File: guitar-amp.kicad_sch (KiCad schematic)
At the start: 62 parts, among them J1 Speaker Output, J2 Input, J3 AC Mains, J4 Screw_Terminal_01x02, J5 Screw_Terminal_01x02, J6 Screw_Terminal_01x02, SW1 SW_SPST, T1 Transformer_1P_1S, T2 Transformer_1P_2S

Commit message: Add lamp and test points
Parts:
- added J7: Lamp, TerminalBlock_RND:TerminalBlock_RND_205-00001_1x02_P5.00mm_Horizontal, symbol Connector:Screw_Terminal_01x02
- added TP1, TP10, TP2, TP3, TP4, TP5, TP6, TP7, TP8, TP9: TestPoint_Probe, TestPoint:TestPoint_Pad_D2.5mm, symbol Connector:TestPoint_Probe
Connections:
- net AC_L: now also J7.1 (Pin_1)
- net AC_N: now also J7.2 (Pin_2)
- net HighDC_227VDC: now also TP6.1
- net HighDC_241VDC: now also TP9.1
- net HighDC_OT: now also TP10.1
- net at C7.2, R11.2, R15.1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: now also TP2.1
- net at J2.T, R10.1, R13.1: now also TP1.1
- net at R12.2, R17.1, V2.7 (G): now also TP3.1
- net HighCurrentTrace1: now reaches J5.2 (Pin_2), R24.1, SW1.1 (A)
- net HighCurrentTrace2: now reaches R22.2, R24.2, SW1.2 (B), V1.4 (F1), V1.5 (F1), V2.4 (F1), V2.5 (F1), V3.4 (F1)
- net HighCurrentTrace2: now also TP7.1
- net at R9.1, V3.2 (G1): now also TP4.1
- net HighCurrentTrace3: now reaches J5.1 (Pin_1), R23.2, V1.9 (F2), V2.9 (F2), V3.5 (F2)
- net HighCurrentTrace3: now also TP8.1
- net at J1.1 (Pin_1), T1.4 (SB): now also TP5.1
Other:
- moved on the sheet: D1, J3, J4, J5, J6, T2

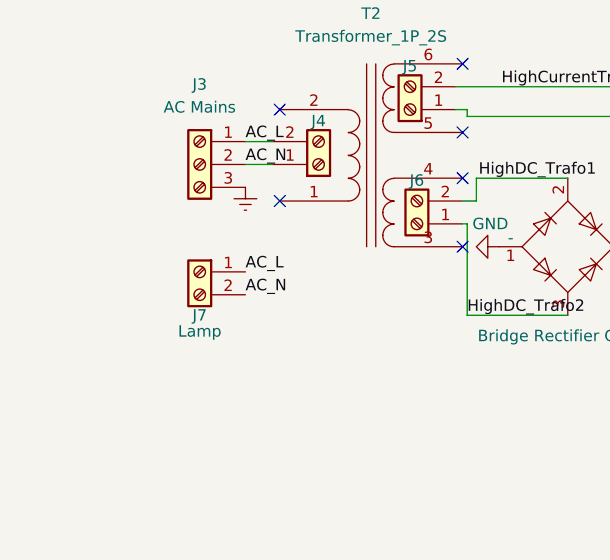
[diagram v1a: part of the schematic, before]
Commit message: Make the filament traces bigger
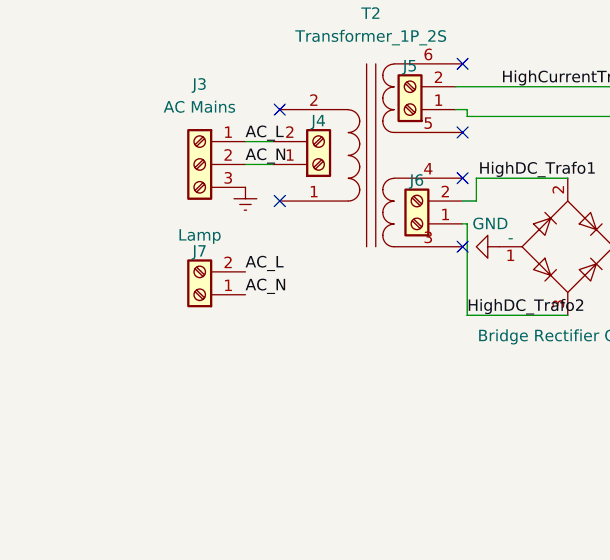
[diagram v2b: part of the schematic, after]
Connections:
- net AC_L: now also J7.2 (Pin_2); no longer J7.1 (Pin_1)
- net AC_N: now also J7.1 (Pin_1); no longer J7.2 (Pin_2)
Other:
- moved on the sheet: J7
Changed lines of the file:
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@@
     (pin "2")
   )
-  (symbol (lib_id "Connector:Screw_Terminal_01x02") (at 37.846 160.02 0) (mirror y) (unit 1)
+  (symbol (lib_id "Connector:Screw_Terminal_01x02") (at 37.846 162.56 180) (unit 1)
     (in_bom yes) (on_board yes)
-    (property "Reference" "J7" (id 0) (at 37.846 164.846 0))
-    (property "Value" "Lamp" (id 1) (at 37.846 166.624 0))
-    (property "Footprint" "TerminalBlock_RND:TerminalBlock_RND_205-00001_1x02_P5.00mm_Horizontal" (id 2) (at 37.846 160.02 0)
+    (property "Reference" "J7" (id 0) (at 37.846 157.734 0))
+    (property "Value" "Lamp" (id 1) (at 37.846 155.956 0))
+    (property "Footprint" "TerminalBlock_RND:TerminalBlock_RND_205-00001_1x02_P5.00mm_Horizontal" (id 2) (at 37.846 162.56 0)
       (effects (font (size 1.27 1.27)) hide)
     )
-    (property "Datasheet" "~" (id 3) (at 37.846 160.02 0)
+    (property "Datasheet" "~" (id 3) (at 37.846 162.56 0)
       (effects (font (size 1.27 1.27)) hide)
     )

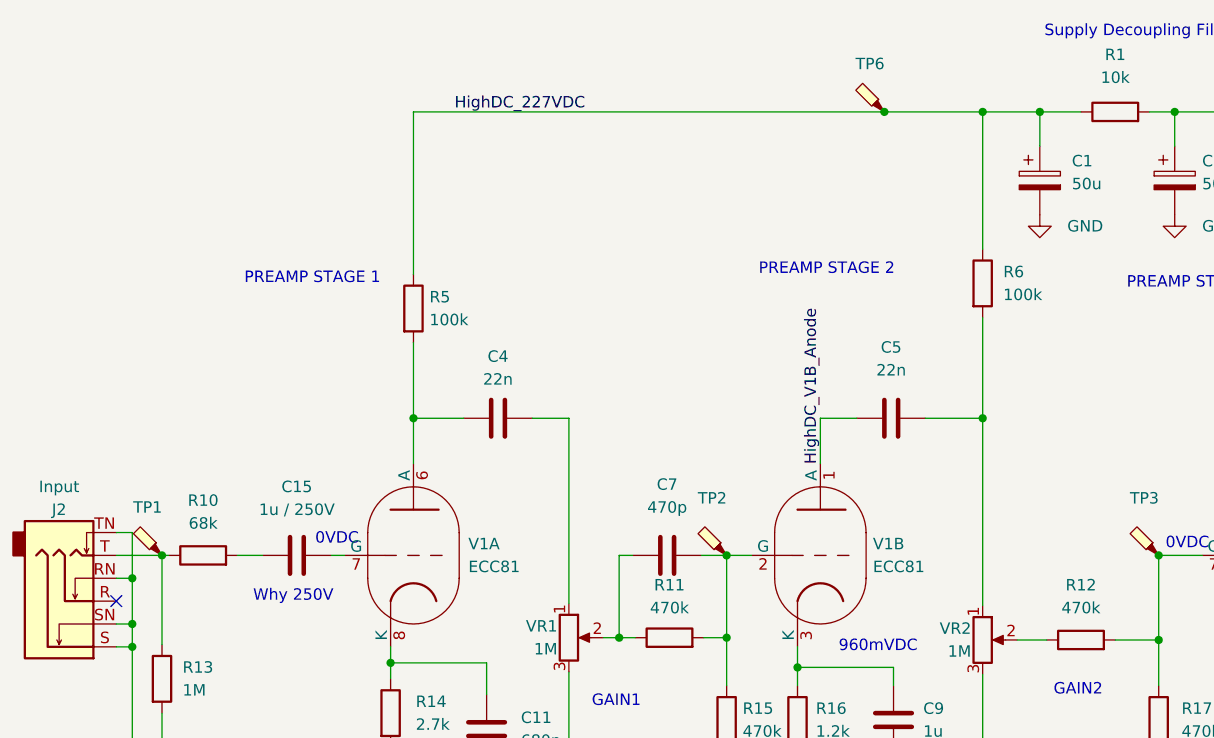
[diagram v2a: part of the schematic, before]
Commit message: Fix R6 and Remove C15
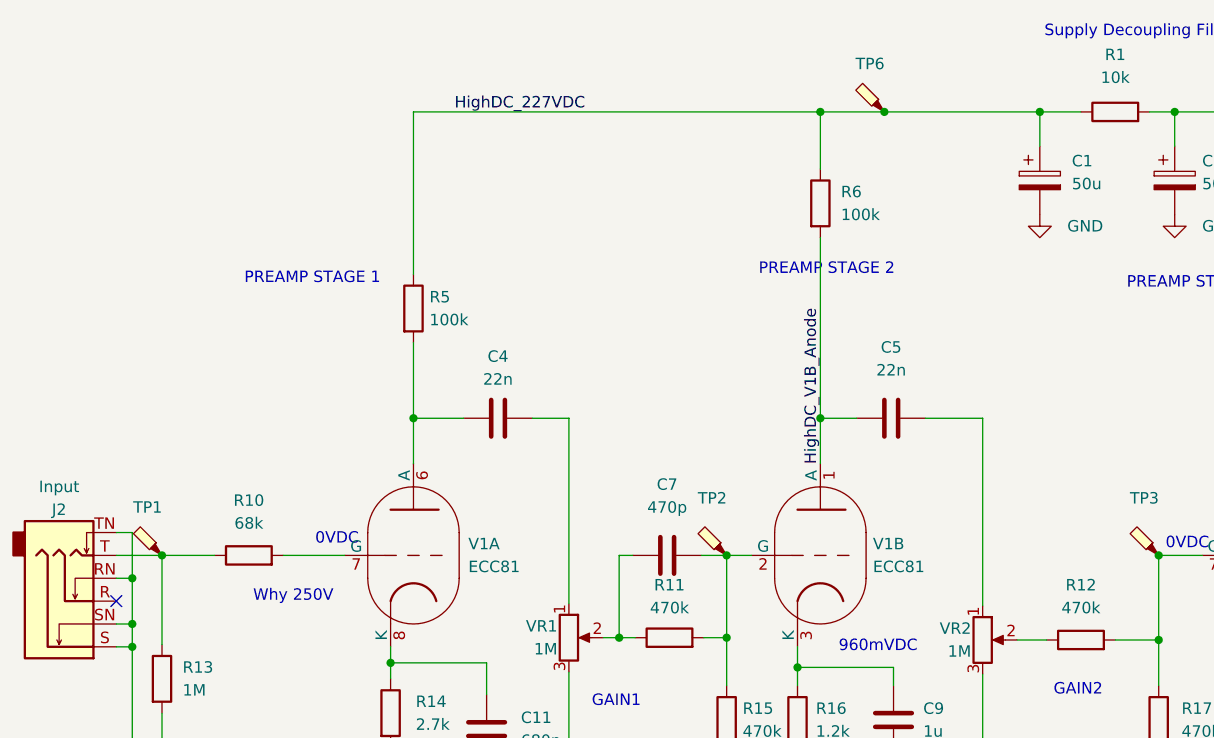
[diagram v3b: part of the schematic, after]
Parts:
- removed C15: 1u / 250V, Capacitor_THT:C_Rect_L27.0mm_W9.0mm_P23.00mm, symbol Device:C
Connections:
- net HighDC_V1B_Anode: now also R6.2
- net at R10.2: now also V1.7 (G)
- net at C5.2, VR2.1: no longer R6.2
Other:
- moved on the sheet: R10, R6
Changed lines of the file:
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@@
   (junction (at 125.476 110.49) (diameter 0) (color 0 0 0 0)
   )
-  (junction (at 125.476 68.58) (diameter 0) (color 0 0 0 0)
-  )
   (junction (at 188.976 139.446) (diameter 0) (color 0 0 0 0)
   )
@@
   (junction (at 146.812 34.544) (diameter 0) (color 0 0 0 0)
   )
-  (junction (at 125.476 34.544) (diameter 0) (color 0 0 0 0)
-  )
   (junction (at 235.458 83.82) (diameter 0) (color 0 0 0 0)
   )
@@
   (junction (at 104.902 96.266) (diameter 0) (color 0 0 0 0)
   )
+  (junction (at 107.442 34.544) (diameter 0) (color 0 0 0 0)
+  )
   (junction (at 34.29 110.49) (diameter 0) (color 0 0 0 0)
   )
@@
   )
   (junction (at 85.09 92.964) (diameter 0) (color 0 0 0 0)
+  )
+  (junction (at 107.442 68.58) (diameter 0) (color 0 0 0 0)
   )
   (junction (at 175.514 60.198) (diameter 0) (color 0 0 0 0)
@@
     (stroke (width 0) (type default) (color 0 0 0 0))
   )
-  (wire (pts (xy 53.086 83.82) (xy 54.61 83.82))
+  (wire (pts (xy 47.752 83.82) (xy 54.61 83.82))
     (stroke (width 0) (type default) (color 0 0 0 0))
   )
@@
     (stroke (width 0) (type default) (color 0 0 0 0))
   )
-  (wire (pts (xy 42.672 83.82) (xy 45.466 83.82))
-    (stroke (width 0) (type default) (color 0 0 0 0))
-  )
   (wire (pts (xy 115.824 155.448) (xy 121.666 155.448))
     (stroke (width 0) (type default) (color 0 0 0 0))
@@
     (stroke (width 0) (type default) (color 0 0 0 0))
   )
-  (wire (pts (xy 62.23 34.544) (xy 114.554 34.544))
+  (wire (pts (xy 62.23 34.544) (xy 107.442 34.544))
     (stroke (width 0) (type default) (color 0 0 0 0))
   )
@@
     (stroke (width 0) (type default) (color 0 0 0 0))
   )
-  (wire (pts (xy 114.554 34.544) (xy 125.476 34.544))
+  (wire (pts (xy 114.554 34.544) (xy 131.826 34.544))
     (stroke (width 0) (type default) (color 0 0 0 0))
   )
@@
     (stroke (width 0) (type default) (color 0 0 0 0))
   )
+  (wire (pts (xy 107.442 40.894) (xy 107.442 34.544))
+    (stroke (width 0) (type default) (color 0 0 0 0))
+  )
   (wire (pts (xy 67.056 154.686) (xy 67.564 154.686))
     (stroke (width 0) (type default) (color 0 0 0 0))
@@
     (stroke (width 0) (type default) (color 0 0 0 0))
   )
-  (wire (pts (xy 34.29 83.82) (xy 35.052 83.82))
+  (wire (pts (xy 34.29 83.82) (xy 40.132 83.82))
     (stroke (width 0) (type default) (color 0 0 0 0))
   )
@@
     (stroke (width 0) (type default) (color 0 0 0 0))
   )
+  (wire (pts (xy 107.442 48.514) (xy 107.442 68.58))
+    (stroke (width 0) (type default) (color 0 0 0 0))
+  )
   (wire (pts (xy 172.72 34.544) (xy 177.292 34.544))
     (stroke (width 0) (type default) (color 0 0 0 0))
@@
     (stroke (width 0) (type default) (color 0 0 0 0))
   )
+  (wire (pts (xy 107.442 34.544) (xy 114.554 34.544))
+    (stroke (width 0) (type default) (color 0 0 0 0))
+  )
   (wire (pts (xy 170.18 58.928) (xy 170.18 60.198))
     (stroke (width 0) (type default) (color 0 0 0 0))
@@
     (stroke (width 0) (type default) (color 0 0 0 0))
   )
-  (wire (pts (xy 125.476 57.404) (xy 125.476 68.58))
-    (stroke (width 0) (type default) (color 0 0 0 0))
-  )
   (wire (pts (xy 249.174 51.054) (xy 249.174 34.544))
     (stroke (width 0) (type default) (color 0 0 0 0))
@@
     (stroke (width 0) (type default) (color 0 0 0 0))
   )
-  (wire (pts (xy 125.476 34.544) (xy 131.826 34.544))
-    (stroke (width 0) (type default) (color 0 0 0 0))
-  )
   (wire (pts (xy 192.278 89.662) (xy 192.278 96.774))
     (stroke (width 0) (type default) (color 0 0 0 0))
@@
   )
   (wire (pts (xy 216.916 138.43) (xy 216.916 142.748))
-    (stroke (width 0) (type default) (color 0 0 0 0))
-  )
-  (wire (pts (xy 125.476 34.544) (xy 125.476 49.784))
     (stroke (width 0) (type default) (color 0 0 0 0))
   )
@@
     (pin "1")
   )
-  (symbol (lib_id "Device:R") (at 38.862 83.82 90) (unit 1)
-    (in_bom yes) (on_board yes) (fields_autoplaced)
-    (property "Reference" "R10" (id 0) (at 38.862 77.724 90))
-    (property "Value" "68k" (id 1) (at 38.862 80.264 90))
-    (property "Footprint" "Resistor_THT:R_Axial_DIN0207_L6.3mm_D2.5mm_P7.62mm_Horizontal" (id 2) (at 38.862 85.598 90)
-      (effects (font (size 1.27 1.27)) hide)
-    )
-    (property "Datasheet" "~" (id 3) (at 38.862 83.82 0)
+  (symbol (lib_id "Device:R") (at 43.942 83.82 90) (unit 1)
+    (in_bom yes) (on_board yes) (fields_autoplaced)
+    (property "Reference" "R10" (id 0) (at 43.942 77.724 90))
+    (property "Value" "68k" (id 1) (at 43.942 80.264 90))
+    (property "Footprint" "Resistor_THT:R_Axial_DIN0207_L6.3mm_D2.5mm_P7.62mm_Horizontal" (id 2) (at 43.942 85.598 90)
+      (effects (font (size 1.27 1.27)) hide)
+    )
+    (property "Datasheet" "~" (id 3) (at 43.942 83.82 0)
       (effects (font (size 1.27 1.27)) hide)
     )
@@
     (pin "3")
   )
-  (symbol (lib_id "Device:R") (at 125.476 53.594 0) (unit 1)
-    (in_bom yes) (on_board yes) (fields_autoplaced)
-    (property "Reference" "R6" (id 0) (at 127.762 52.3239 0)
-      (effects (font (size 1.27 1.27)) (justify left))
-    )
-    (property "Value" "100k" (id 1) (at 127.762 54.8639 0)
-      (effects (font (size 1.27 1.27)) (justify left))
-    )
-    (property "Footprint" "Resistor_THT:R_Axial_DIN0207_L6.3mm_D2.5mm_P7.62mm_Horizontal" (id 2) (at 123.698 53.594 90)
-      (effects (font (size 1.27 1.27)) hide)
-    )
-    (property "Datasheet" "~" (id 3) (at 125.476 53.594 0)
+  (symbol (lib_id "Device:R") (at 107.442 44.704 0) (unit 1)
+    (in_bom yes) (on_board yes) (fields_autoplaced)
+    (property "Reference" "R6" (id 0) (at 109.728 43.4339 0)
+      (effects (font (size 1.27 1.27)) (justify left))
+    )
+    (property "Value" "100k" (id 1) (at 109.728 45.9739 0)
+      (effects (font (size 1.27 1.27)) (justify left))
+    )
+    (property "Footprint" "Resistor_THT:R_Axial_DIN0207_L6.3mm_D2.5mm_P7.62mm_Horizontal" (id 2) (at 105.664 44.704 90)
+      (effects (font (size 1.27 1.27)) hide)
+    )
+    (property "Datasheet" "~" (id 3) (at 107.442 44.704 0)
       (effects (font (size 1.27 1.27)) hide)
     )
@@
     (pin "2")
   )
-  (symbol (lib_id "Device:C") (at 49.276 83.82 90) (unit 1)
-    (in_bom yes) (on_board yes) (fields_autoplaced)
-    (property "Reference" "C15" (id 0) (at 49.276 76.2 90))
-    (property "Value" "1u / 250V" (id 1) (at 49.276 78.74 90))
-    (property "Footprint" "Capacitor_THT:C_Rect_L27.0mm_W9.0mm_P23.00mm" (id 2) (at 53.086 82.8548 0)
-      (effects (font (size 1.27 1.27)) hide)
-    )
-    (property "Datasheet" "~" (id 3) (at 49.276 83.82 0)
-      (effects (font (size 1.27 1.27)) hide)
-    )
-    (pin "1")
-    (pin "2")
-  )
   (symbol (lib_id "Device:C_Polarized") (at 99.822 160.528 0) (unit 1)
     (in_bom yes) (on_board yes) (fields_autoplaced)
@@
       (reference "C14") (unit 1) (value "50u") (footprint "Capacitor_THT:CP_Radial_D16.0mm_P7.50mm")
     )
-    (path "/b375741c-d524-4718-8b51-0b70caa17dd3"
-      (reference "C15") (unit 1) (value "1u / 250V") (footprint "Capacitor_THT:C_Rect_L27.0mm_W9.0mm_P23.00mm")
-    )
     (path "/12fd4662-2da1-4a2a-8e7b-b1a611b506f3"

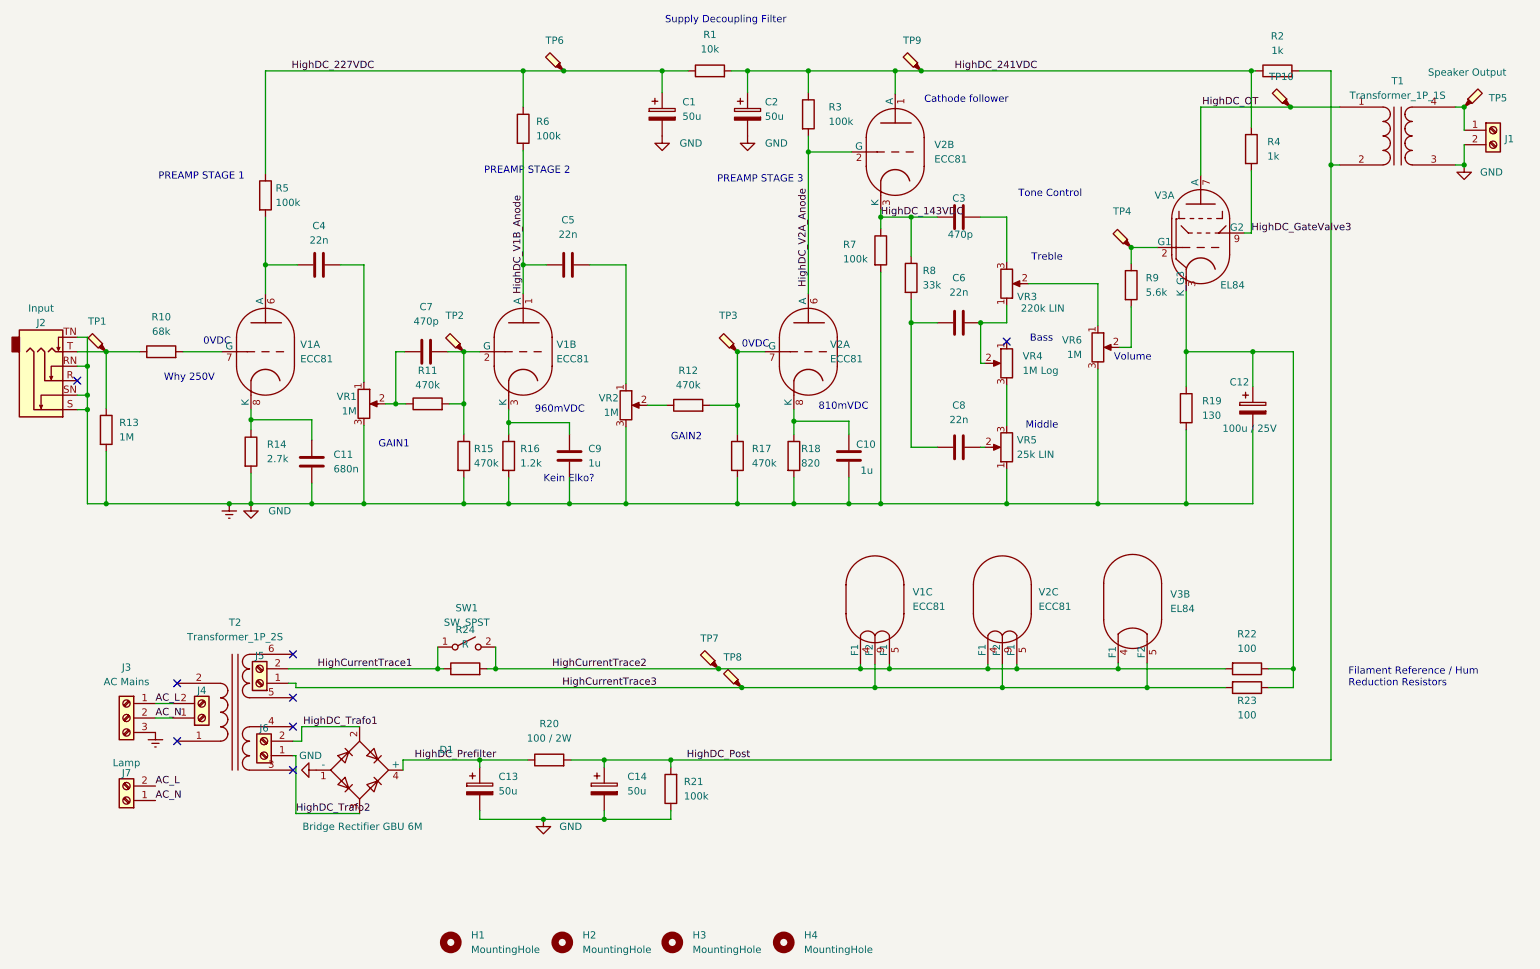
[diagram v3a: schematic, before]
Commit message: Self latching circuit for soft start
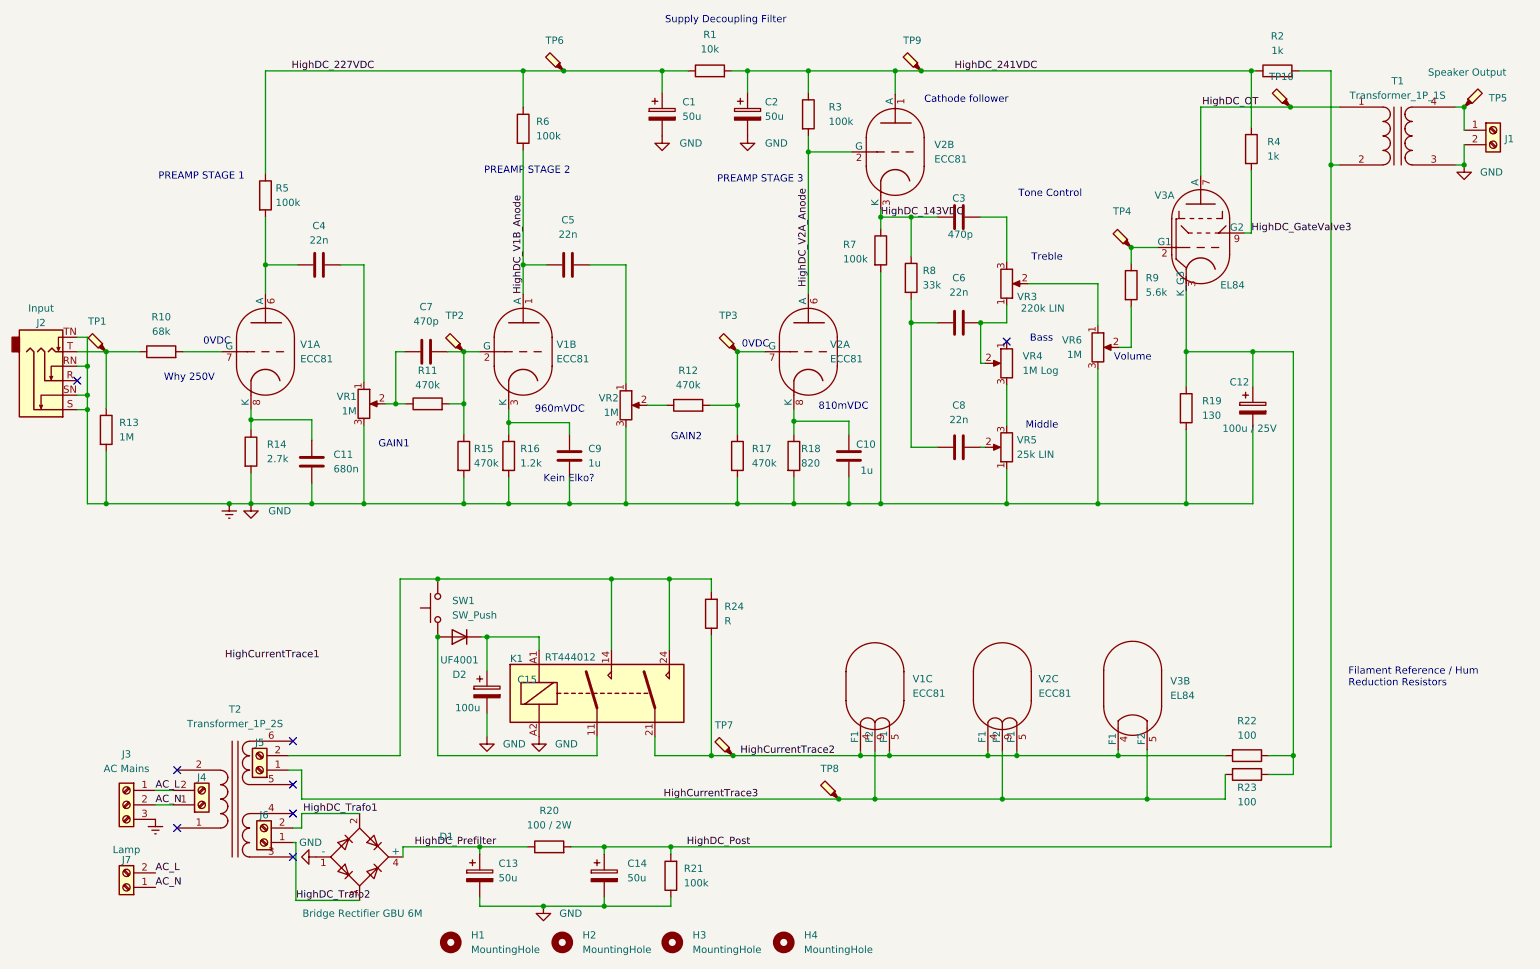
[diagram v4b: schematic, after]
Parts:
- removed SW1: SW_SPST, Button_Switch_THT:SW_CuK_JS202011CQN_DPDT_Straight, symbol Switch:SW_SPST
- added C15: 100u, symbol Device:C_Polarized
- added D2: UF4001, Diode_THT:D_DO-41_SOD81_P10.16mm_Horizontal, symbol Diode:1N4001
- added K1: RT444012, Relay_THT:Relay_DPST_Schrack-RT2-FormA_RM5mm, symbol Relay:RT44xxxx
- added SW1: SW_Push, Button_Switch_THT:SW_Tactile_SPST_Angled_PTS645Vx58-2LFS, symbol Switch:SW_Push
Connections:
- net Earth: now also C15.2, K1.A2
- net HighCurrentTrace1: no longer J5.2 (Pin_2), R24.1
- net HighCurrentTrace2: now also R24.1, K1.21; no longer R24.2
- new net: J5.2 (Pin_2), K1.14, K1.24, R24.2, SW1.2
- new net: C15.1, D2.1 (K), K1.A1
- new net: D2.2 (A), K1.11, SW1.1
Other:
- moved on the sheet: C13, C14, D1, J3, J4, J5, J6, J7, R20, R21, R22, R23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
